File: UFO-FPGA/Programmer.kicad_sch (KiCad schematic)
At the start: 41 parts, among them U2 FT2232HL, U3 ASDMB-12MHz, U5 93LC56CT-I/MS

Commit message: footprints and PCB
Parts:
- D3, D4: footprint (none) -> LED_SMD:LED_0805_2012Metric_Pad1.15x1.40mm_HandSolder
- R1, R10, R11, R12, R13, R14, R15, R16, R17, R18, R19, R2, R20, R3, R33, R34, R4, R5, R6, R7, R8, R9: footprint (none) -> Resistor_SMD:R_0805_2012Metric_Pad1.20x1.40mm_HandSolder
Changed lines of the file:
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@@
       (effects (font (size 1.27 1.27)))
     )
-    (property "Footprint" "" (at 307.34 144.018 90)
+    (property "Footprint" "Resistor_SMD:R_0805_2012Metric_Pad1.20x1.40mm_HandSolder" (at 307.34 144.018 90)
       (effects (font (size 1.27 1.27)) hide)
     )
@@
       (effects (font (size 1.27 1.27)))
     )
-    (property "Footprint" "" (at 307.34 100.838 90)
+    (property "Footprint" "Resistor_SMD:R_0805_2012Metric_Pad1.20x1.40mm_HandSolder" (at 307.34 100.838 90)
       (effects (font (size 1.27 1.27)) hide)
     )
@@
       (effects (font (size 1.27 1.27)))
     )
-    (property "Footprint" "" (at 307.34 131.318 90)
+    (property "Footprint" "Resistor_SMD:R_0805_2012Metric_Pad1.20x1.40mm_HandSolder" (at 307.34 131.318 90)
       (effects (font (size 1.27 1.27)) hide)
     )
@@
       (effects (font (size 1.27 1.27)))
     )
-    (property "Footprint" "" (at 307.34 93.218 90)
+    (property "Footprint" "Resistor_SMD:R_0805_2012Metric_Pad1.20x1.40mm_HandSolder" (at 307.34 93.218 90)
       (effects (font (size 1.27 1.27)) hide)
     )
@@
       (effects (font (size 1.27 1.27)))
     )
-    (property "Footprint" "" (at 307.34 128.778 90)
+    (property "Footprint" "Resistor_SMD:R_0805_2012Metric_Pad1.20x1.40mm_HandSolder" (at 307.34 128.778 90)
       (effects (font (size 1.27 1.27)) hide)
     )
@@
       (effects (font (size 1.27 1.27)))
     )
-    (property "Footprint" "" (at 134.62 156.718 90)
+    (property "Footprint" "Resistor_SMD:R_0805_2012Metric_Pad1.20x1.40mm_HandSolder" (at 134.62 156.718 90)
       (effects (font (size 1.27 1.27)) hide)
     )
@@
       (effects (font (size 1.27 1.27)))
     )
-    (property "Footprint" "" (at 316.23 156.718 90)
+    (property "Footprint" "Resistor_SMD:R_0805_2012Metric_Pad1.20x1.40mm_HandSolder" (at 316.23 156.718 90)
       (effects (font (size 1.27 1.27)) hide)
     )
@@
       (effects (font (size 1.27 1.27)))
     )
-    (property "Footprint" "" (at 122.428 137.795 90)
+    (property "Footprint" "Resistor_SMD:R_0805_2012Metric_Pad1.20x1.40mm_HandSolder" (at 122.428 137.795 90)
       (effects (font (size 1.27 1.27)) hide)
     )
@@
       (effects (font (size 1.27 1.27)))
     )
-    (property "Footprint" "" (at 307.34 85.598 90)
+    (property "Footprint" "Resistor_SMD:R_0805_2012Metric_Pad1.20x1.40mm_HandSolder" (at 307.34 85.598 90)
       (effects (font (size 1.27 1.27)) hide)
     )
@@
       (effects (font (size 1.27 1.27)))
     )
-    (property "Footprint" "" (at 307.34 88.138 90)
+    (property "Footprint" "Resistor_SMD:R_0805_2012Metric_Pad1.20x1.40mm_HandSolder" (at 307.34 88.138 90)
       (effects (font (size 1.27 1.27)) hide)
     )
@@
       (effects (font (size 1.27 1.27)))
     )
-    (property "Footprint" "" (at 307.34 83.058 90)
+    (property "Footprint" "Resistor_SMD:R_0805_2012Metric_Pad1.20x1.40mm_HandSolder" (at 307.34 83.058 90)
       (effects (font (size 1.27 1.27)) hide)
     )
@@
       (effects (font (size 1.27 1.27)))
     )
-    (property "Footprint" "" (at 208.28 112.522 90)
+    (property "Footprint" "Resistor_SMD:R_0805_2012Metric_Pad1.20x1.40mm_HandSolder" (at 208.28 112.522 90)
       (effects (font (size 1.27 1.27)) hide)
     )
@@
       (effects (font (size 1.27 1.27)))
     )
-    (property "Footprint" "" (at 306.07 162.56 0)
+    (property "Footprint" "LED_SMD:LED_0805_2012Metric_Pad1.15x1.40mm_HandSolder" (at 306.07 162.56 0)
       (effects (font (size 1.27 1.27)) hide)
     )
@@
       (effects (font (size 1.27 1.27)))
     )
-    (property "Footprint" "" (at 307.34 138.938 90)
+    (property "Footprint" "Resistor_SMD:R_0805_2012Metric_Pad1.20x1.40mm_HandSolder" (at 307.34 138.938 90)
       (effects (font (size 1.27 1.27)) hide)
     )
@@
       (effects (font (size 1.27 1.27)))
     )
-    (property "Footprint" "" (at 186.69 193.04 90)
+    (property "Footprint" "Resistor_SMD:R_0805_2012Metric_Pad1.20x1.40mm_HandSolder" (at 186.69 193.04 90)
       (effects (font (size 1.27 1.27)) hide)
     )
@@
       (effects (font (size 1.27 1.27)))
     )
-    (property "Footprint" "" (at 307.34 141.478 90)
+    (property "Footprint" "Resistor_SMD:R_0805_2012Metric_Pad1.20x1.40mm_HandSolder" (at 307.34 141.478 90)
       (effects (font (size 1.27 1.27)) hide)
     )
@@
       (effects (font (size 1.27 1.27)))
     )
-    (property "Footprint" "" (at 307.34 98.298 90)
+    (property "Footprint" "Resistor_SMD:R_0805_2012Metric_Pad1.20x1.40mm_HandSolder" (at 307.34 98.298 90)
       (effects (font (size 1.27 1.27)) hide)
     )
@@
       (effects (font (size 1.27 1.27)))
     )
-    (property "Footprint" "" (at 208.28 121.158 90)
+    (property "Footprint" "Resistor_SMD:R_0805_2012Metric_Pad1.20x1.40mm_HandSolder" (at 208.28 121.158 90)
       (effects (font (size 1.27 1.27)) hide)
     )
@@
       (effects (font (size 1.27 1.27)))
     )
-    (property "Footprint" "" (at 135.128 137.795 90)
+    (property "Footprint" "Resistor_SMD:R_0805_2012Metric_Pad1.20x1.40mm_HandSolder" (at 135.128 137.795 90)
       (effects (font (size 1.27 1.27)) hide)
     )
@@
       (effects (font (size 1.27 1.27)))
     )
-    (property "Footprint" "" (at 316.23 160.782 90)
+    (property "Footprint" "Resistor_SMD:R_0805_2012Metric_Pad1.20x1.40mm_HandSolder" (at 316.23 160.782 90)
       (effects (font (size 1.27 1.27)) hide)
     )
@@
       (effects (font (size 1.27 1.27)))
     )
-    (property "Footprint" "" (at 306.07 154.94 0)
+    (property "Footprint" "LED_SMD:LED_0805_2012Metric_Pad1.15x1.40mm_HandSolder" (at 306.07 154.94 0)
       (effects (font (size 1.27 1.27)) hide)
     )
@@
       (effects (font (size 1.27 1.27)))
     )
-    (property "Footprint" "" (at 307.34 133.858 90)
+    (property "Footprint" "Resistor_SMD:R_0805_2012Metric_Pad1.20x1.40mm_HandSolder" (at 307.34 133.858 90)
       (effects (font (size 1.27 1.27)) hide)
     )
@@
       (effects (font (size 1.27 1.27)))
     )
-    (property "Footprint" "" (at 307.34 136.398 90)
+    (property "Footprint" "Resistor_SMD:R_0805_2012Metric_Pad1.20x1.40mm_HandSolder" (at 307.34 136.398 90)
       (effects (font (size 1.27 1.27)) hide)
     )
@@
       (effects (font (size 1.27 1.27)))
     )
-    (property "Footprint" "" (at 128.778 137.795 90)
-      (effects (font (size 1.27 1.27)) hide)
-    )
+    (property "Footprint" "Resistor_SMD:R_0805_2012Metric_Pad1.20x1.40mm_HandSolder" (at 128.778 137.795 90)
+      (effects (font (size 1.27 1.27)) hide)
+    )

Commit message: footprint
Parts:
- C1, C10, C11, C12, C13, C14, C2, C3, C4, C5, C6, C7, C8, C9: footprint (none) -> Capacitor_SMD:C_0805_2012Metric_Pad1.18x1.45mm_HandSolder
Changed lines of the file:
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@@
       (effects (font (size 1.27 1.27)) (justify left))
     )
-    (property "Footprint" "" (at 176.2252 36.83 0)
+    (property "Footprint" "Capacitor_SMD:C_0805_2012Metric_Pad1.18x1.45mm_HandSolder" (at 176.2252 36.83 0)
       (effects (font (size 1.27 1.27)) hide)
     )
@@
       (effects (font (size 1.27 1.27)) (justify right))
     )
-    (property "Footprint" "" (at 249.8598 37.465 0)
+    (property "Footprint" "Capacitor_SMD:C_0805_2012Metric_Pad1.18x1.45mm_HandSolder" (at 249.8598 37.465 0)
       (effects (font (size 1.27 1.27)) hide)
     )
@@
       (effects (font (size 1.27 1.27)) (justify left))
     )
-    (property "Footprint" "" (at 167.3352 36.83 0)
+    (property "Footprint" "Capacitor_SMD:C_0805_2012Metric_Pad1.18x1.45mm_HandSolder" (at 167.3352 36.83 0)
       (effects (font (size 1.27 1.27)) hide)
     )
@@
       (effects (font (size 1.27 1.27)) (justify left))
     )
-    (property "Footprint" "" (at 260.6548 37.465 0)
+    (property "Footprint" "Capacitor_SMD:C_0805_2012Metric_Pad1.18x1.45mm_HandSolder" (at 260.6548 37.465 0)
       (effects (font (size 1.27 1.27)) hide)
     )
@@
       (effects (font (size 1.27 1.27)) (justify left))
     )
-    (property "Footprint" "" (at 194.6402 36.83 0)
+    (property "Footprint" "Capacitor_SMD:C_0805_2012Metric_Pad1.18x1.45mm_HandSolder" (at 194.6402 36.83 0)
       (effects (font (size 1.27 1.27)) hide)
     )
@@
       (effects (font (size 1.27 1.27)) (justify left))
     )
-    (property "Footprint" "" (at 184.4802 111.125 0)
+    (property "Footprint" "Capacitor_SMD:C_0805_2012Metric_Pad1.18x1.45mm_HandSolder" (at 184.4802 111.125 0)
       (effects (font (size 1.27 1.27)) hide)
     )
@@
       (effects (font (size 1.27 1.27)) (justify left))
     )
-    (property "Footprint" "" (at 195.2752 111.125 0)
+    (property "Footprint" "Capacitor_SMD:C_0805_2012Metric_Pad1.18x1.45mm_HandSolder" (at 195.2752 111.125 0)
       (effects (font (size 1.27 1.27)) hide)
     )
@@
       (effects (font (size 1.27 1.27)) (justify left))
     )
-    (property "Footprint" "" (at 204.1652 36.83 0)
+    (property "Footprint" "Capacitor_SMD:C_0805_2012Metric_Pad1.18x1.45mm_HandSolder" (at 204.1652 36.83 0)
       (effects (font (size 1.27 1.27)) hide)
     )
@@
       (effects (font (size 1.27 1.27)) (justify left))
     )
-    (property "Footprint" "" (at 86.0552 160.02 0)
+    (property "Footprint" "Capacitor_SMD:C_0805_2012Metric_Pad1.18x1.45mm_HandSolder" (at 86.0552 160.02 0)
       (effects (font (size 1.27 1.27)) hide)
     )
@@
       (effects (font (size 1.27 1.27)) (justify left))
     )
-    (property "Footprint" "" (at 180.0352 175.895 0)
+    (property "Footprint" "Capacitor_SMD:C_0805_2012Metric_Pad1.18x1.45mm_HandSolder" (at 180.0352 175.895 0)
       (effects (font (size 1.27 1.27)) hide)
     )
@@
       (effects (font (size 1.27 1.27)) (justify left))
     )
-    (property "Footprint" "" (at 221.9452 36.83 0)
+    (property "Footprint" "Capacitor_SMD:C_0805_2012Metric_Pad1.18x1.45mm_HandSolder" (at 221.9452 36.83 0)
       (effects (font (size 1.27 1.27)) hide)
     )
@@
       (effects (font (size 1.27 1.27)) (justify left))
     )
-    (property "Footprint" "" (at 158.4452 36.83 0)
+    (property "Footprint" "Capacitor_SMD:C_0805_2012Metric_Pad1.18x1.45mm_HandSolder" (at 158.4452 36.83 0)
       (effects (font (size 1.27 1.27)) hide)
     )
@@
       (effects (font (size 1.27 1.27)) (justify left))
     )
-    (property "Footprint" "" (at 232.7402 36.83 0)
+    (property "Footprint" "Capacitor_SMD:C_0805_2012Metric_Pad1.18x1.45mm_HandSolder" (at 232.7402 36.83 0)
       (effects (font (size 1.27 1.27)) hide)
     )
@@
       (effects (font (size 1.27 1.27)) (justify left))
     )
-    (property "Footprint" "" (at 185.7502 36.83 0)
-      (effects (font (size 1.27 1.27)) hide)
-    )
+    (property "Footprint" "Capacitor_SMD:C_0805_2012Metric_Pad1.18x1.45mm_HandSolder" (at 185.7502 36.83 0)
+      (effects (font (size 1.27 1.27)) hide)
+    )

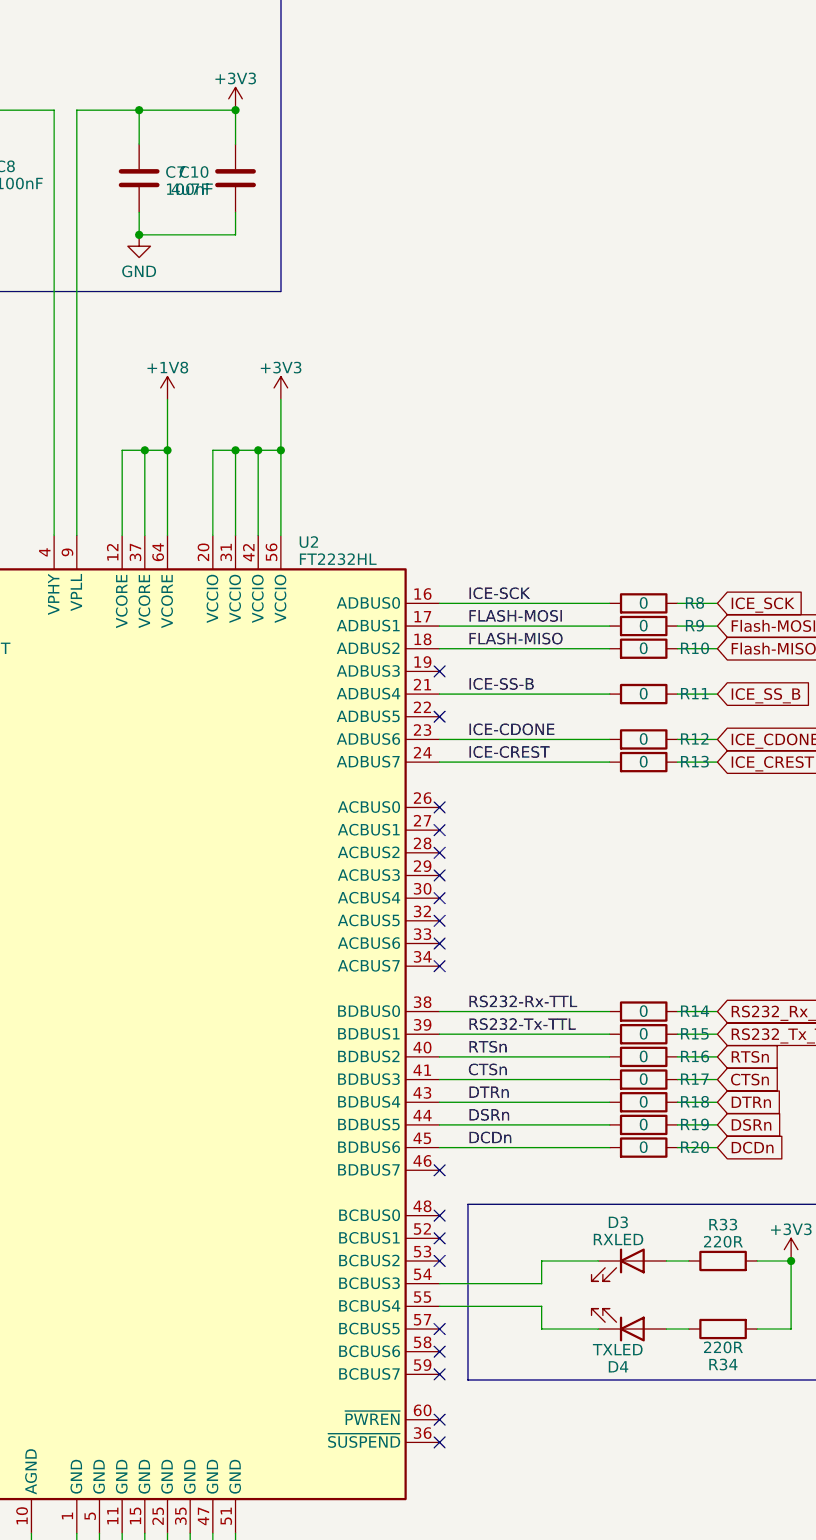
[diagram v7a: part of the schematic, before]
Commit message: PCB planes
Added:
added Power plane +1v2, +3v3 and +5v on layer 4
Ground plane on layer 2 and 5
Added signal layer 1,3 and 6
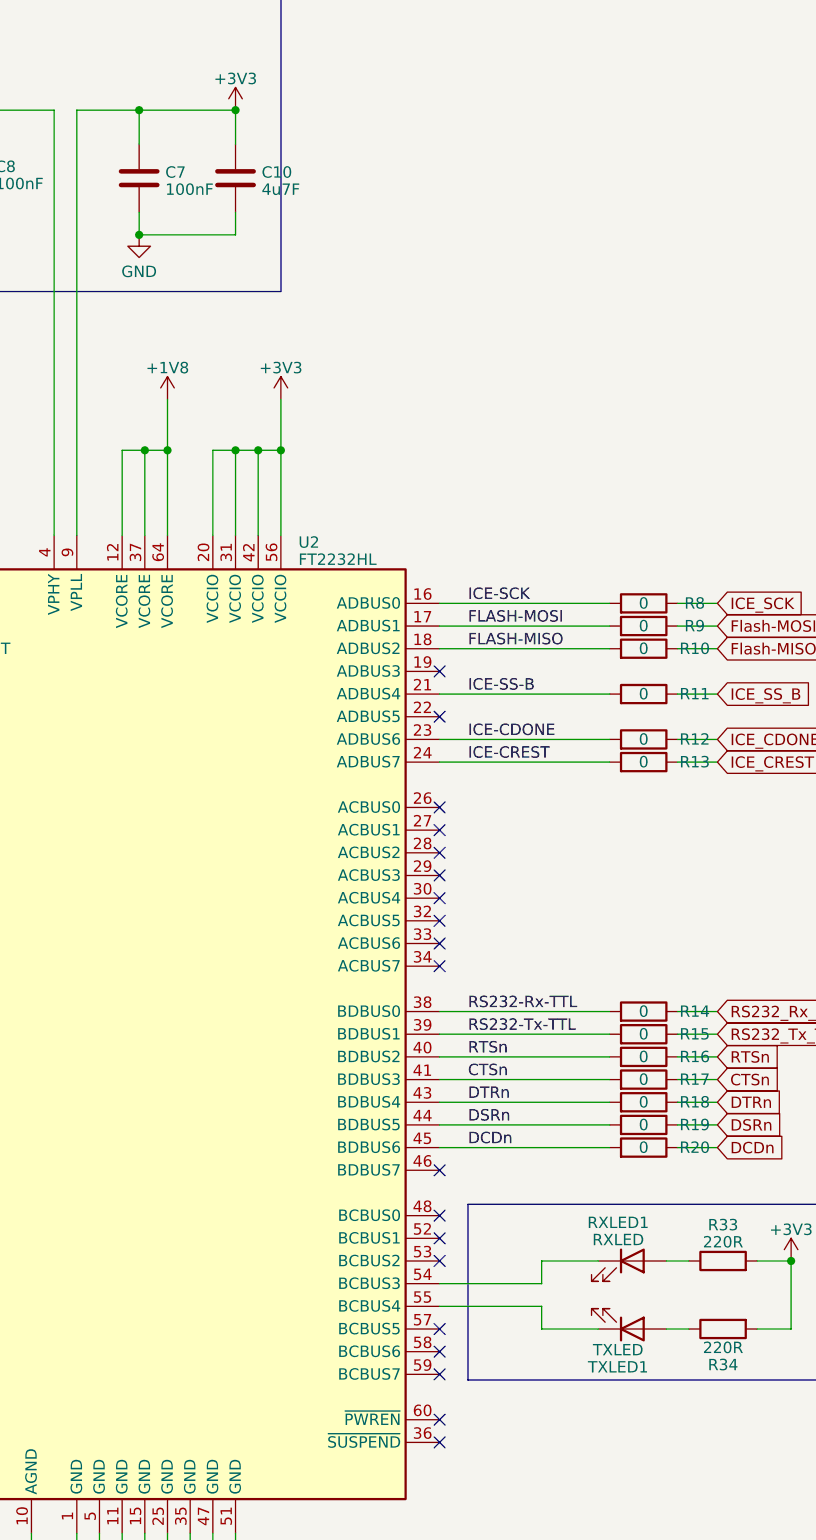
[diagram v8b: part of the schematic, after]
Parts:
- renumbered D3 to RXLED1, D4 to TXLED1
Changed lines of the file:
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@@
     )
   )
-  (symbol (lib_id "Device:C") (at 261.62 33.655 0) (mirror y) (unit 1)
-    (in_bom yes) (on_board yes) (dnp no) (fields_autoplaced)
-    (property "Reference" "C10" (at 258.699 33.0113 0)
-      (effects (font (size 1.27 1.27)) (justify left))
-    )
-    (property "Value" "4u7F" (at 258.699 34.9323 0)
-      (effects (font (size 1.27 1.27)) (justify left))
-    )
-    (property "Footprint" "Capacitor_SMD:C_0805_2012Metric_Pad1.18x1.45mm_HandSolder" (at 260.6548 37.465 0)
+  (symbol (lib_id "Device:C") (at 261.62 33.655 0) (unit 1)
+    (in_bom yes) (on_board yes) (dnp no)
+    (property "Reference" "C10" (at 264.541 33.0113 0)
+      (effects (font (size 1.27 1.27)) (justify left))
+    )
+    (property "Value" "4u7F" (at 264.541 34.9323 0)
+      (effects (font (size 1.27 1.27)) (justify left))
+    )
+    (property "Footprint" "Capacitor_SMD:C_0805_2012Metric_Pad1.18x1.45mm_HandSolder" (at 262.5852 37.465 0)
       (effects (font (size 1.27 1.27)) hide)
     )
@@
   (symbol (lib_id "Device:LED") (at 306.07 162.56 0) (mirror x) (unit 1)
     (in_bom yes) (on_board yes) (dnp no)
-    (property "Reference" "D4" (at 304.4825 166.8399 0)
+    (property "Reference" "TXLED1" (at 304.4825 166.8399 0)
       (effects (font (size 1.27 1.27)))
     )
@@
       (project "UFO-FPGA"
         (path "/b3168f6a-c732-41d3-aeeb-d97dd2f1bb65/eec89a79-dace-443c-aa86-713b48a49f95"
-          (reference "D4") (unit 1)
+          (reference "TXLED1") (unit 1)
         )
       )
@@
   (symbol (lib_id "Device:LED") (at 306.07 154.94 0) (unit 1)
     (in_bom yes) (on_board yes) (dnp no) (fields_autoplaced)
-    (property "Reference" "D3" (at 304.4825 150.6601 0)
+    (property "Reference" "RXLED1" (at 304.4825 150.6601 0)
       (effects (font (size 1.27 1.27)))
     )
@@
       (project "UFO-FPGA"
         (path "/b3168f6a-c732-41d3-aeeb-d97dd2f1bb65/eec89a79-dace-443c-aa86-713b48a49f95"
-          (reference "D3") (unit 1)
-        )
-      )
+          (reference "RXLED1") (unit 1)
+        )
+      )
